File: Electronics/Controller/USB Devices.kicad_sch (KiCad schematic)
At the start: 20 parts, among them U10 FT232RL, U11 FT232RL, U12 FT232RL, U13 FT232RL

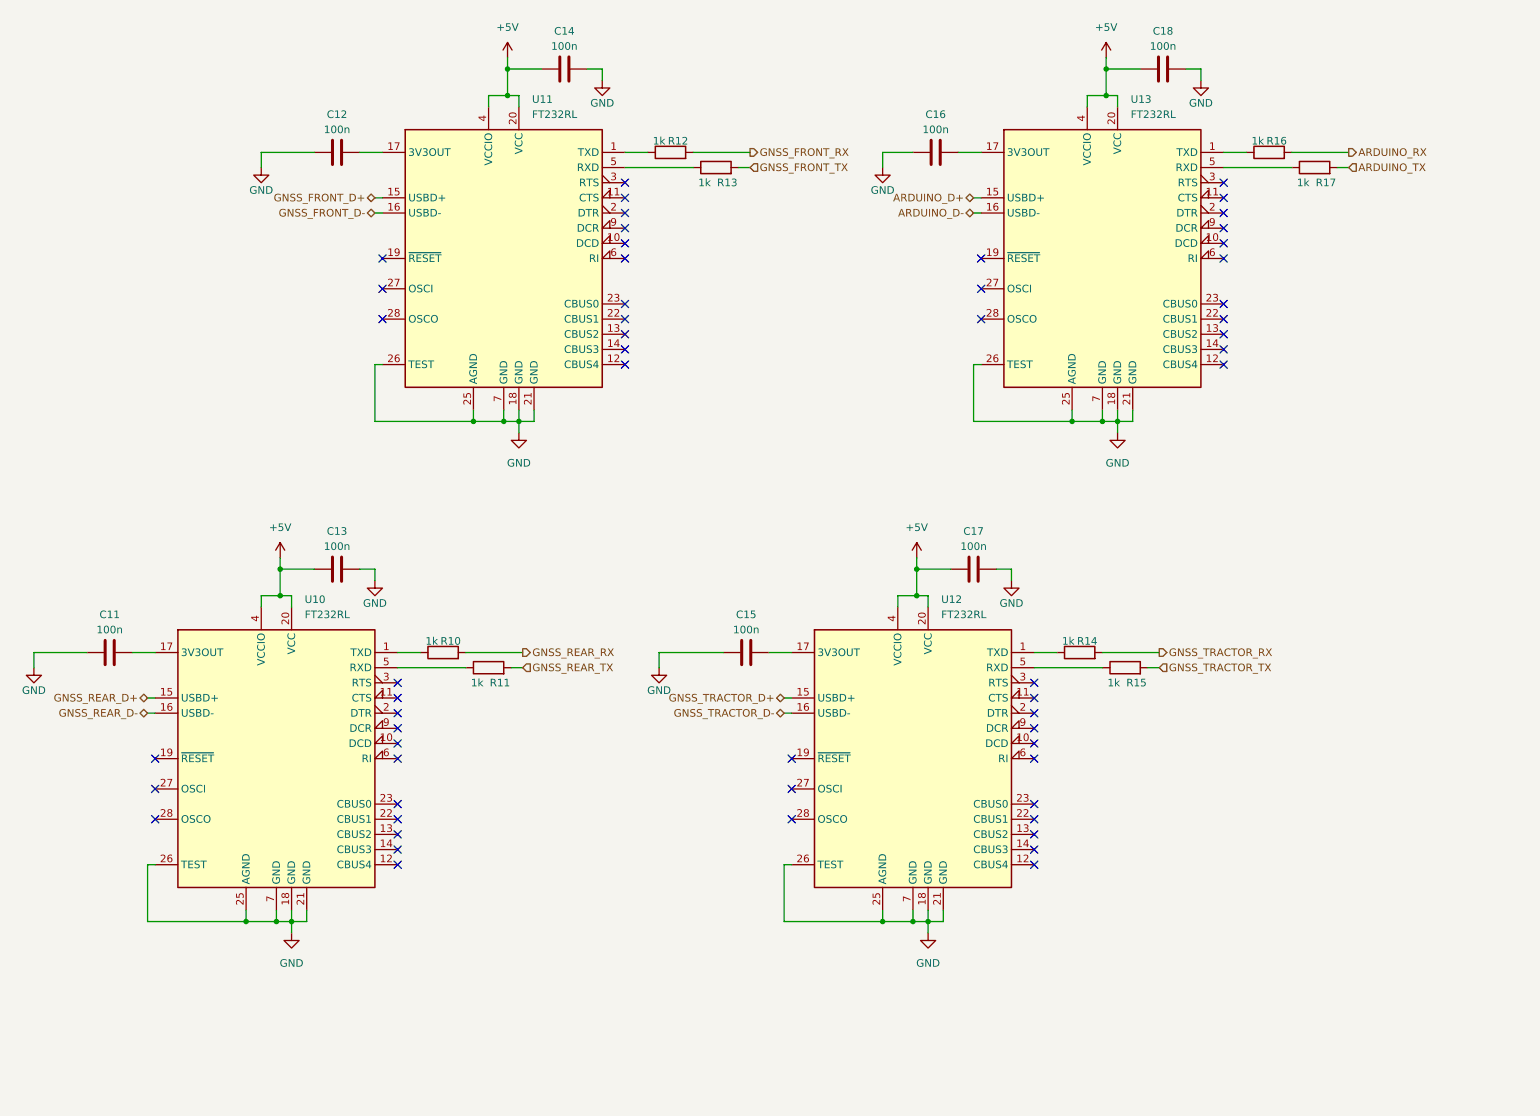
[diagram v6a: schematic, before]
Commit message: Added 4.7uF caps to FT232RL on controller.
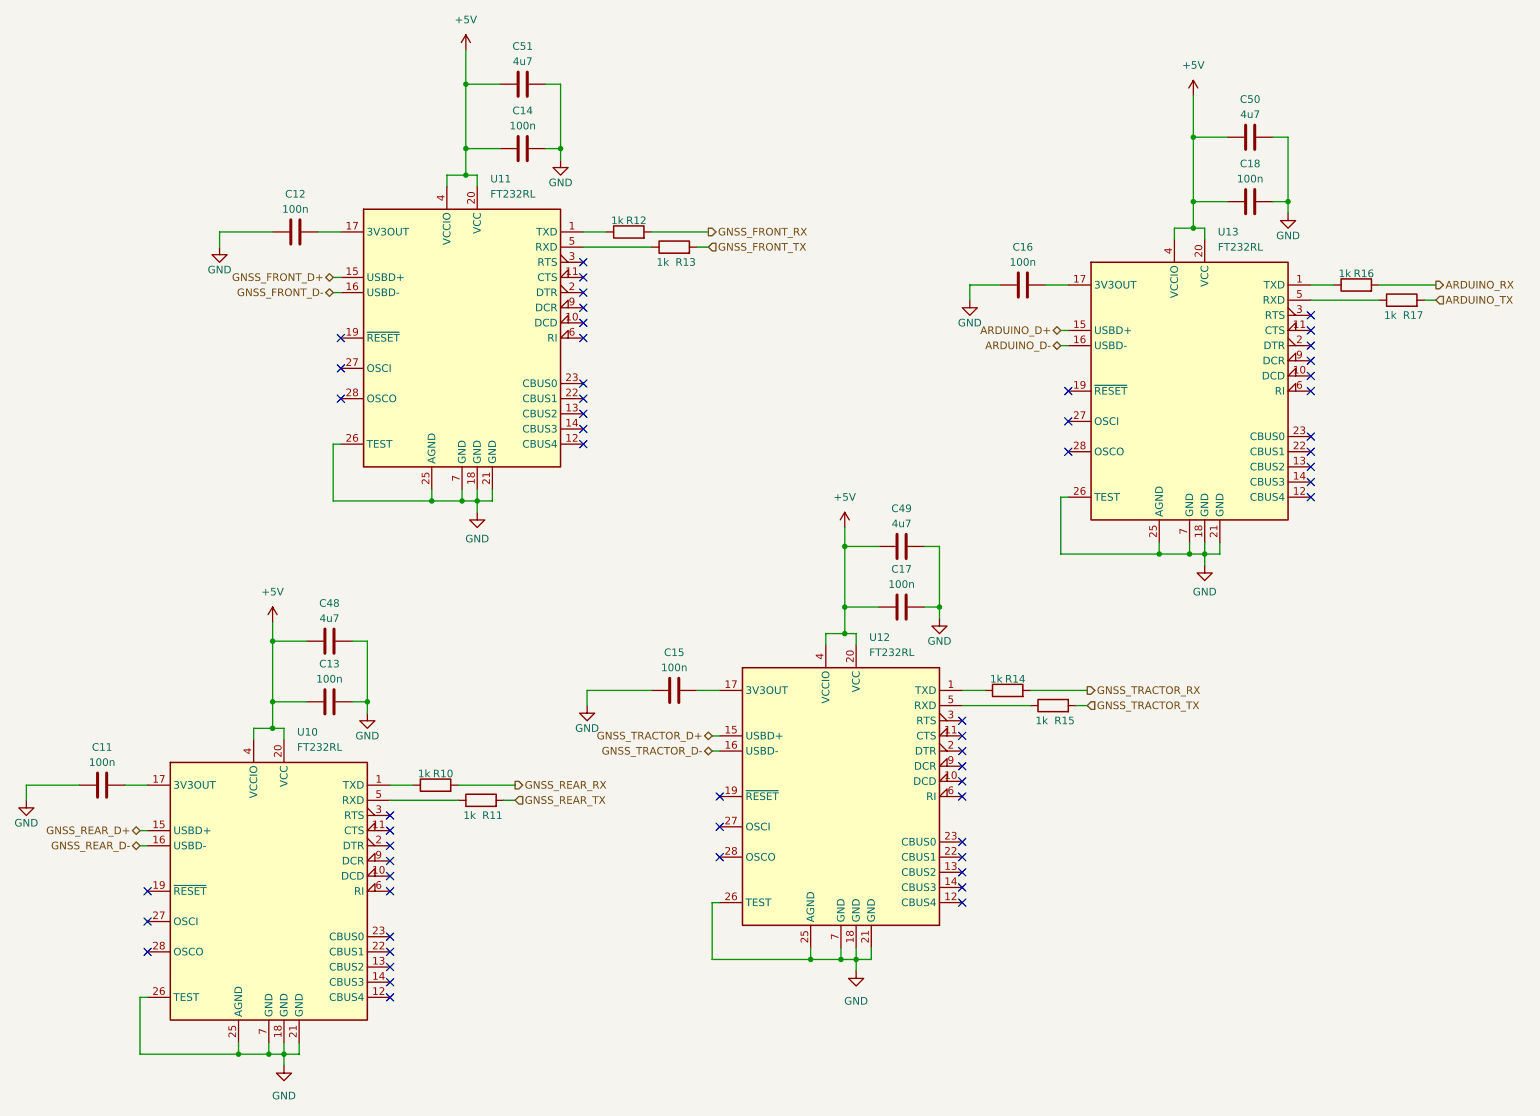
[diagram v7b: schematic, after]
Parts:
- added C48, C49, C50, C51: 4u7, Capacitor_SMD:C_0805_2012Metric, symbol Device:C
- C11, C12, C13, C14, C15, C16, C17, C18: LCSC (none) -> C1711
- R10, R11, R12, R13, R14, R15, R16, R17: LCSC (none) -> C17513
- U10, U11, U12, U13: LCSC (none) -> C8690
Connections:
- net +5V: now also C48.1, C49.1, C50.1, C51.1
- net GND: now also C48.2, C49.2, C50.2, C51.2
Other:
- moved on the sheet: C11, C12, C13, C14, C15, C16, C17, C18, R10, R11, R12, R13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

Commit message: Removed JLCPCB part numbers for Teensy and BNO085 connectors. Added JLCPCB part number for 4.7uF capacitor. Generated JLCPCB manufacturing files for all boards.
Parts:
- C48, C49, C50, C51: LCSC (none) -> C1779
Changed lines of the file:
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@@
       (effects (font (size 1.27 1.27)) hide)
     )
-    (property "LCSC" "" (at 163.83 103.505 0)
+    (property "LCSC" "C1779" (at 163.83 103.505 0)
       (effects (font (size 1.27 1.27)) hide)
     )
@@
       (effects (font (size 1.27 1.27)) hide)
     )
-    (property "LCSC" "" (at 100.33 26.035 0)
+    (property "LCSC" "C1779" (at 100.33 26.035 0)
       (effects (font (size 1.27 1.27)) hide)
     )
@@
       (effects (font (size 1.27 1.27)) hide)
     )
-    (property "LCSC" "" (at 67.945 119.38 0)
+    (property "LCSC" "C1779" (at 67.945 119.38 0)
       (effects (font (size 1.27 1.27)) hide)
     )
@@
       (effects (font (size 1.27 1.27)) hide)
     )
-    (property "LCSC" "" (at 222.25 34.925 0)
-      (effects (font (size 1.27 1.27)) hide)
-    )
+    (property "LCSC" "C1779" (at 222.25 34.925 0)
+      (effects (font (size 1.27 1.27)) hide)
+    )
